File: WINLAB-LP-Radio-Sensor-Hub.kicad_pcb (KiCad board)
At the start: 2 copper layers, 65 x 55 mm, 74 parts, among them J1 FTSH-105-01-L-DV-K-A, J2 USB_C_Receptacle_USB2.0_16P, J3 Conn_01x02, J4 Conn_Coaxial, J5 Conn_Coaxial, J6 Conn_01x05, J7 Conn_01x05, J8 Conn_01x05, J9 Conn_01x05, Q1 AO3401A, Q2 AO3401A, U1 EFR32FG23L020F128GM40-C, U2 Si7021-A20, U3 CN3063, U4 TLV74033PDBVR, U5 CH340N, U6 TPS7A0522PDBV, U7 ADG902BRMZ, Y1 39MHz 10pF

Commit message: minor tweaks, BOM
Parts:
- moved G*** 2.23 mm to (228.1, 43.2)
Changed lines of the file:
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@@
 	(footprint "LOGO"
 		(layer "F.Cu")
-		(at 225.885358 43.488446)
+		(at 228.1 43.2)
 		(property "Reference" "G***"
 			(at 0 0 0)
@@
 	)
 	(gr_text "r0 • Cy Westbrook • Jun 2026"
-		(at 215.885358 47.188446 0)
+		(at 218.1 46.9 0)
 		(layer "F.SilkS")
 		(effects
@@
 	)
 	(gr_text "ULP Radio Sensor Hub"
-		(at 215.885358 45.688446 0)
+		(at 218.1 45.4 0)
 		(layer "F.SilkS" knockout)
 		(effects

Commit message: r0 final
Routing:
- net GND: vias 212 -> 211
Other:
- outline, holes or cut-outs redrawn
- board text added: "LP Radio Sensor Hub"
- board text removed: "ULP Radio Sensor Hub"

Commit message: preliminary JLCPCB BOM, some initial changes for r1
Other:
- board text added: "INSERTING BATTERY UPSIDE DOWN MAY CAUSE IRREVERSABLE DAMAGE"

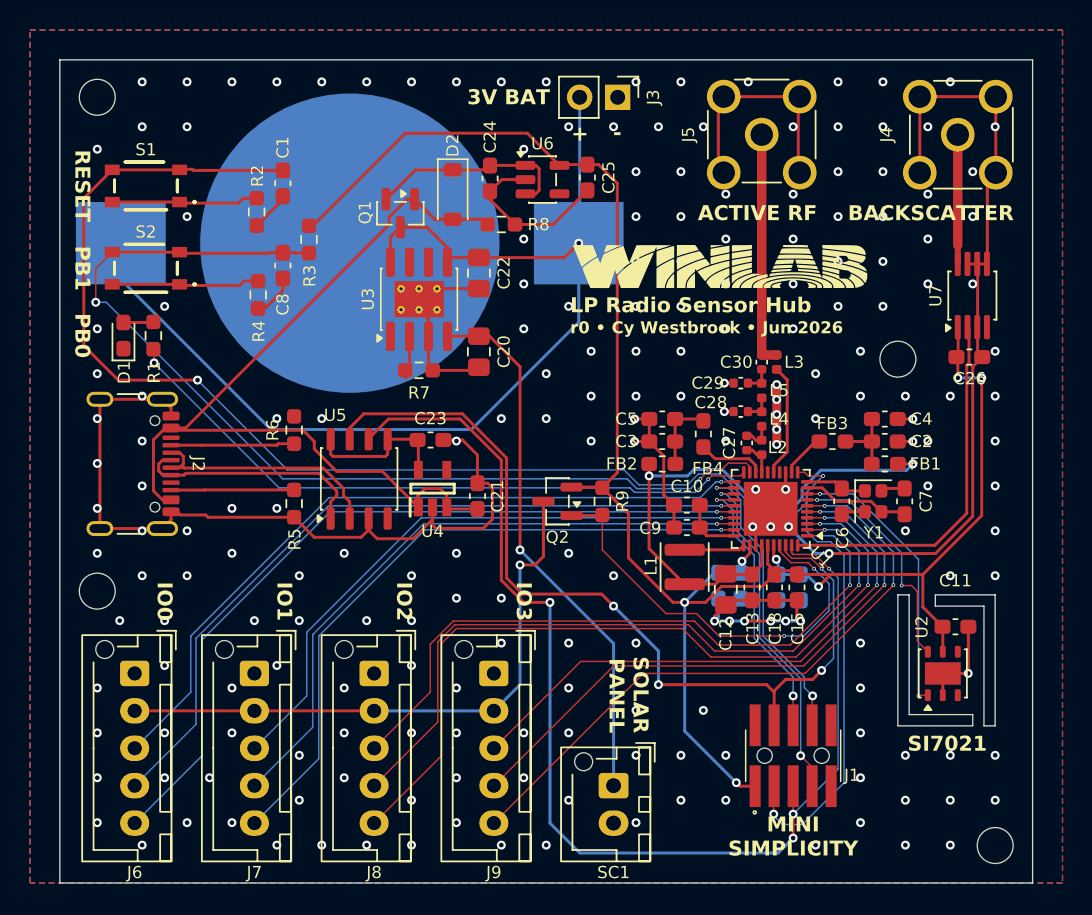
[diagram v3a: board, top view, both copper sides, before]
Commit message: USB charging, UVP HW supervisor, PAVDD selection, charger IC enable jumper, layout and silkscreen changes
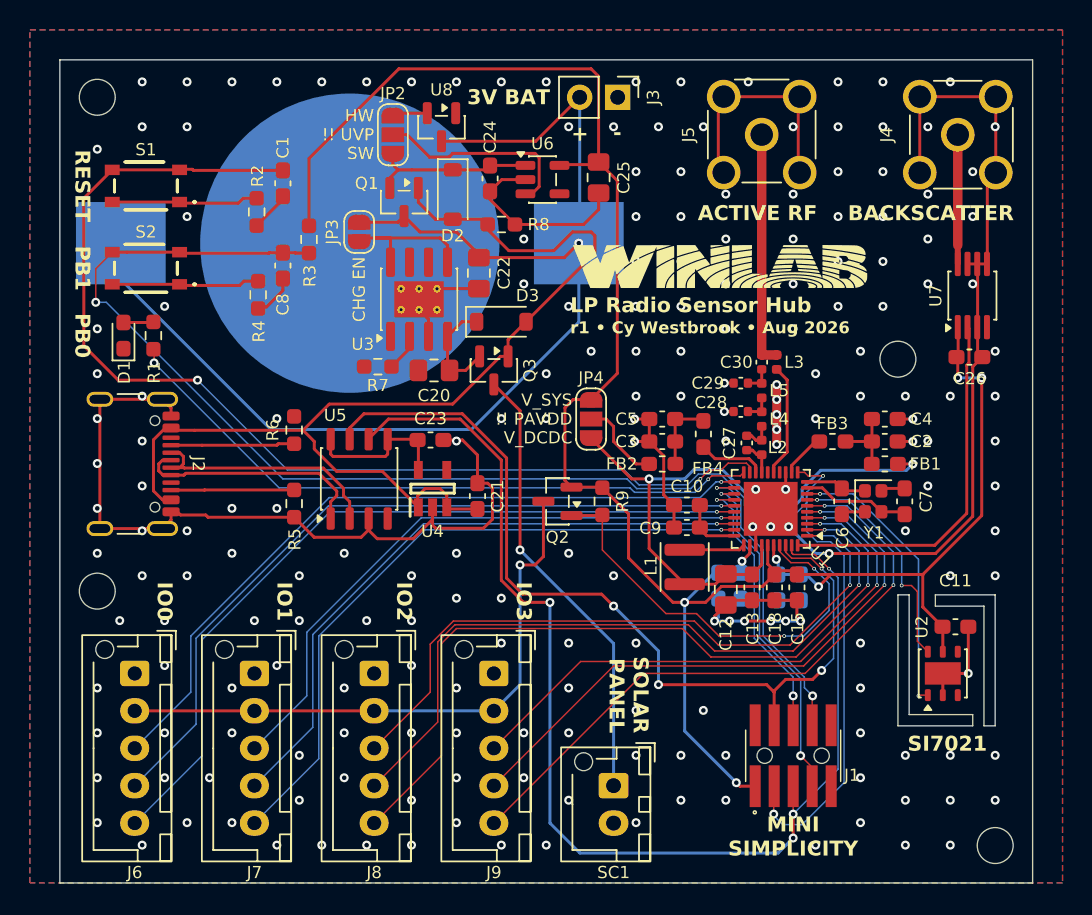
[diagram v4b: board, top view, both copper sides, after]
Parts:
- added D3: 1N4148W, Diode_SMD:D_SOD-123, F.Cu at (213.5, 46.5)
- added JP2: SolderJumper_3_Open, Jumper:SolderJumper-3_P1.3mm_Open_RoundedPad1.0x1.5mm, F.Cu at (206.2, 34.0)
- added JP3: SolderJumper_2_Open, Jumper:SolderJumper-2_P1.3mm_Open_RoundedPad1.0x1.5mm, F.Cu at (204.0, 40.5)
- added JP4: SolderJumper_3_Open, Jumper:SolderJumper-3_P1.3mm_Open_RoundedPad1.0x1.5mm, F.Cu at (219.5, 53.0)
- added Q3: AO3401A, Package_TO_SOT_SMD:SOT-23, F.Cu at (213.0, 49.8)
- added U8: TPS3839K33DBZ, Package_TO_SOT_SMD:SOT-23, F.Cu at (209.5, 33.5)
- C22: value 4.7u -> 22u
- C25: value 1u -> 22u; footprint Capacitor_SMD:C_0603_1608Metric_Pad1.08x0.95mm_HandSolder -> Capacitor_SMD:C_0805_2012Metric_Pad1.18x1.45mm_HandSolder
- U6: value TPS7A0522PDBV -> TPS7A0533PDBV
- moved C20 3.25 mm to (209.0, 49.8), turned to 180 degrees
- moved R7 2.76 mm to (205.2, 49.5), turned to 180 degrees
- moved Q1 0.79 mm to (207.0, 38.5)
- moved C25 0.75 mm to (220.0, 36.9)
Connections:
- C20 pad 1: V_SOLAR -> Net-(D3-K)
- FB2 pad 1: EFR32_DCDC -> Net-(JP4-C)
- J1 pad 4: VCOM_RX -> VCOM_TX
- J1 pad 5: VCOM_TX -> VCOM_RX
- U3 pad 4: V_SOLAR -> Net-(D3-K)
- U3 pad 5: V_BAT -> Net-(JP3-A)
- U3 pad 8: V_BAT -> Net-(JP3-A)
- U6 pad 3: Net-(D2-K) -> Net-(JP2-C)
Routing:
- net +V_SYS: track 130.3 -> 144.3 mm
- net Net-(JP2-C): track 0.00 -> 13.7 mm
- net V_USB: track 59.8 -> 72.4 mm
- net V_BAT: track 71.8 -> 82.2 mm
- net Net-(JP3-A): track 0.00 -> 10.1 mm
- net Net-(D3-K): track 0.00 -> 7.08 mm
- net V_SOLAR: track 36.3 -> 30.1 mm
- net Net-(JP4-C): track 0.00 -> 5.70 mm
- net GND: track 200.4 -> 196.1 mm, vias 211 -> 206
- net EFR32_DCDC: track 37.0 -> 41.2 mm
- net Net-(D2-K): track 13.7 -> 11.3 mm
- net Net-(JP2-A): track 0.00 -> 2.36 mm
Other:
- board text added: "!! PAVDD"
- board text added: "!! UVP"
- board text added: "CHG EN"
- board text added: "HW"
- board text added: "SW"
- board text added: "USE BATTERY TYPE LIR2450 3.7V RECHARGEABLE"
- board text added: "V_DCDC"
- board text added: "V_SYS"
- board text added: "r1 • Cy Westbrook • Aug 2026"
- board text removed: "r0 • Cy Westbrook • Jun 2026"
